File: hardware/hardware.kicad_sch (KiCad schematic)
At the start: 100 parts, among them J1 Conn_Coaxial, J10 Conn_Coaxial, J11 Conn_01x06_Pin, J2 BOOT, J3 SWD, J4 Conn_Coaxial, J5 Conn_Coaxial, J6 Conn_Coaxial, J7 Conn_Coaxial, J8 Conn_Coaxial, J9 Conn_Coaxial, SW1 SW_Push, U11 24LC32, U13 24LC32, U15 24LC32, U17 24LC32, U2 STM32F103C8Tx, U3 24LC32, U5 24LC32, U7 24LC32, U9 24LC32, Y2 Crystal_GND24

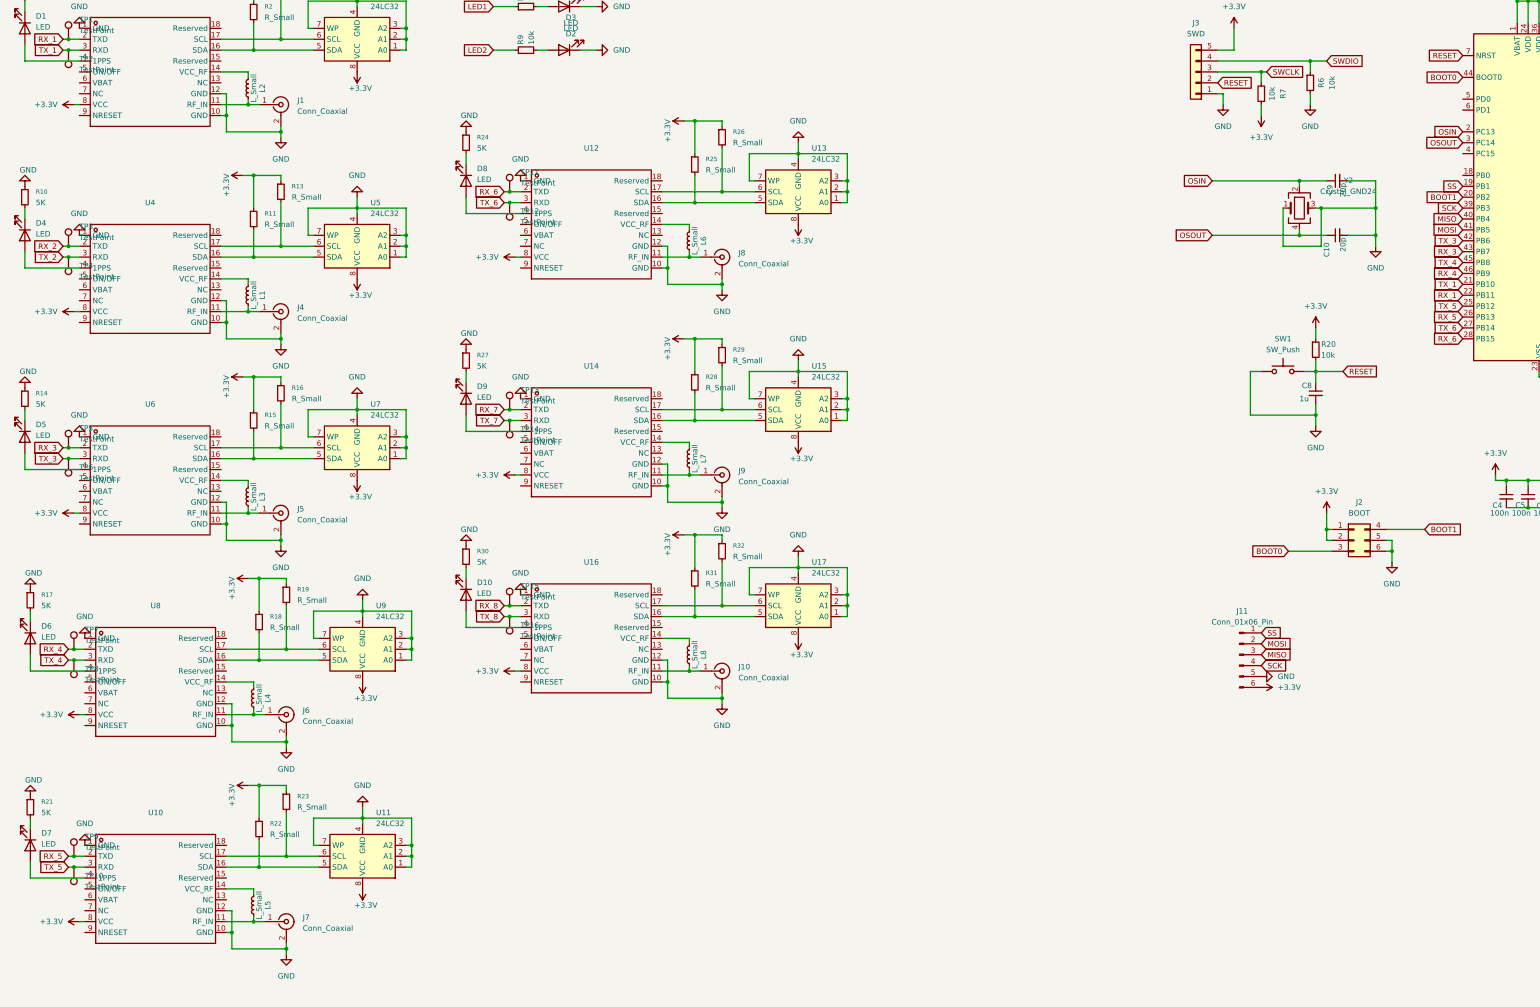
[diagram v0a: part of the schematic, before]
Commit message: add GM capacitor + vbat to 3.3 + move osc on correct pins on stm32
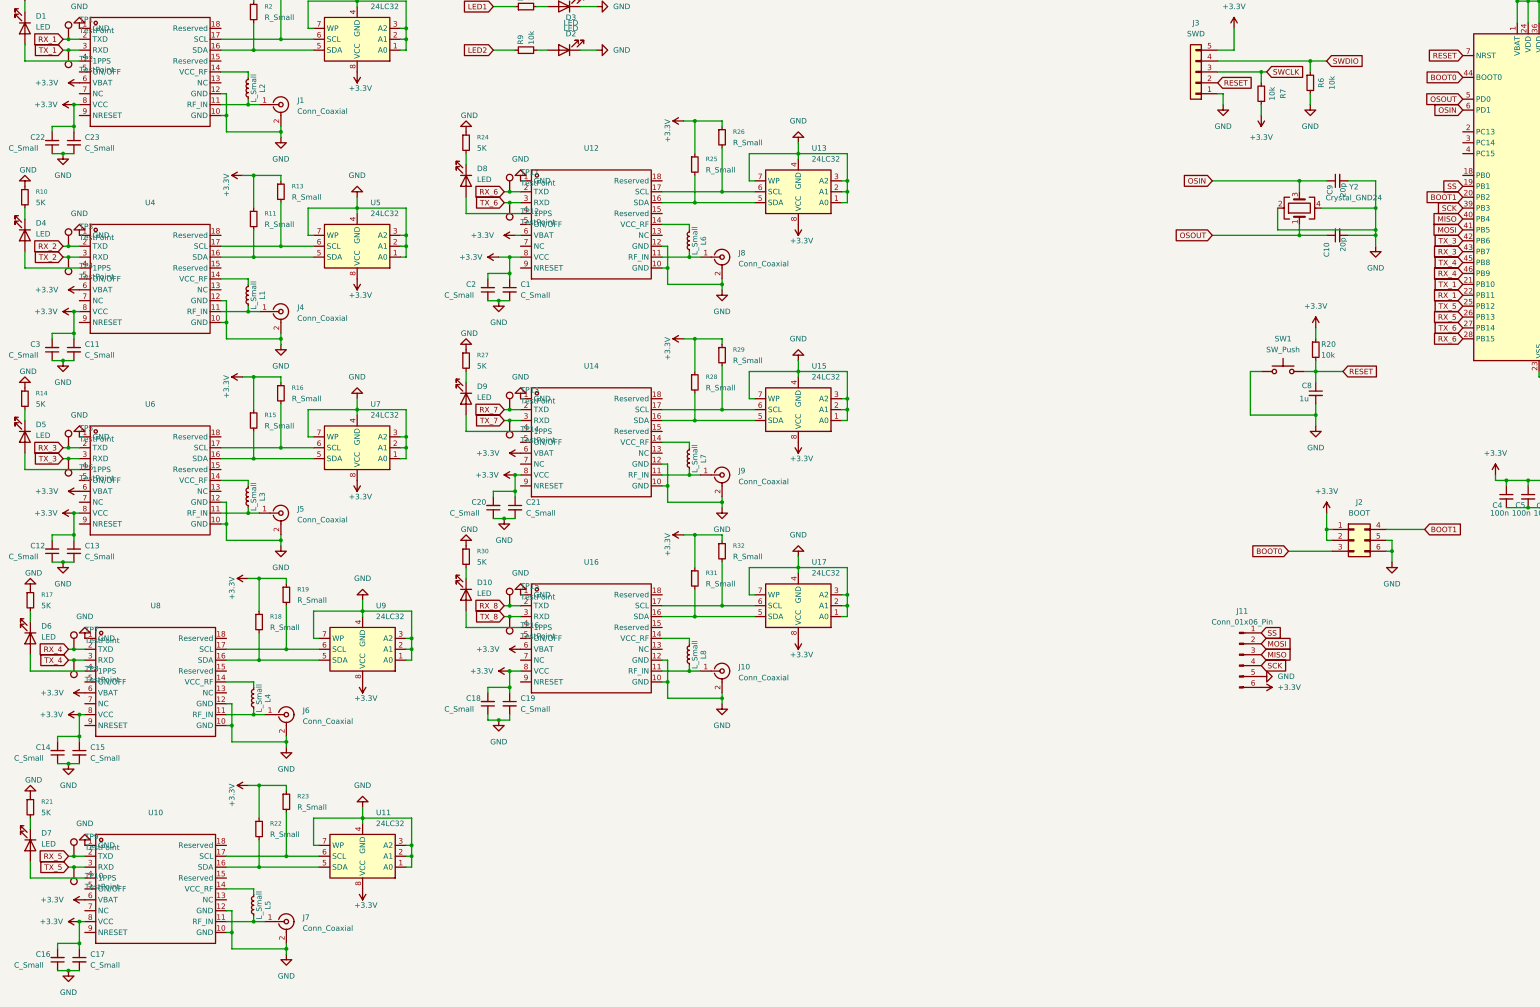
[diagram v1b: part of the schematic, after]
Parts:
- added C1, C11, C13, C15, C17, C19, C21, C23: C_Small, Capacitor_SMD:C_0603_1608Metric, symbol Device:C_Small
- added C12, C14, C16, C18, C2, C20, C22, C3: C_Small, Capacitor_SMD:C_1206_3216Metric, symbol Device:C_Small
- U1, U10, U12, U14, U16, U4, U6, U8: value ~ -> (none)
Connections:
- net +3.3V: now also U1.6 (VBAT), U10.6 (VBAT), U12.6 (VBAT), U14.6 (VBAT), U16.6 (VBAT), U4.6 (VBAT), U6.6 (VBAT), U8.6 (VBAT), C1.1, C11.1, C12.2, C13.1, C14.2, C15.1, C16.2, C17.1, C18.2, C19.1, C2.2, C20.2, C21.1, C22.2, C23.1, C3.2
- net GND: now also Y2.2, Y2.4, C1.2, C11.2, C12.1, C13.2, C14.1, C15.2, C16.1, C17.2, C18.1, C19.2, C2.1, C20.1, C21.2, C22.1, C23.2, C3.1; no longer Y2.1, Y2.3
- net OSIN: now also U2.6 (PD1), Y2.3; no longer U2.2 (PC13), Y2.2
- net OSOUT: now also U2.5 (PD0), Y2.1; no longer U2.3 (PC14), Y2.4
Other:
- moved on the sheet: Y2

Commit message: fix swdio programming
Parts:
- removed R6, R7: 10k, Resistor_SMD:R_0603_1608Metric, symbol Device:R_Small
